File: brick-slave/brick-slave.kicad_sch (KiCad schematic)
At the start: 4 parts, among them J1 Conn_01x06_Male, J2 Conn_01x06_Male, J3 Conn_01x06_Female, J4 Conn_01x06_Female

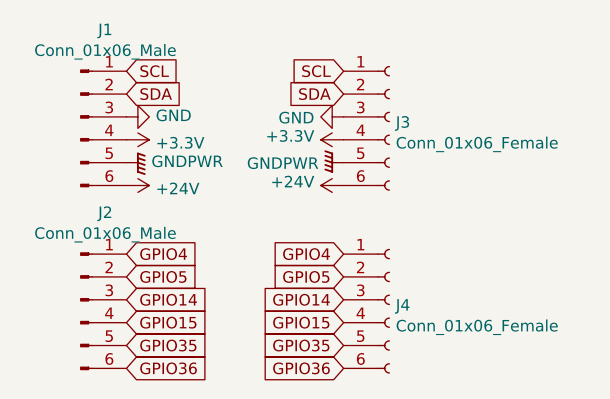
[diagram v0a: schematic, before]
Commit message: change PWR voltage
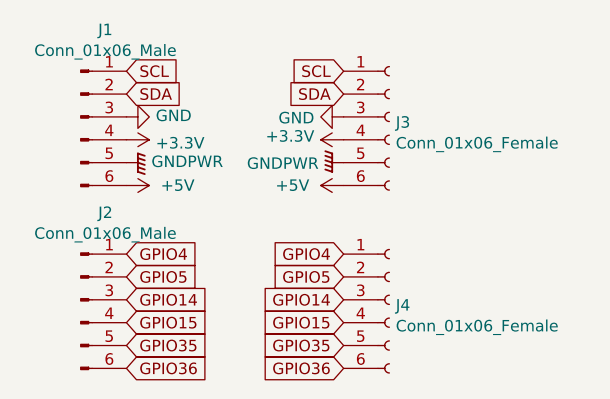
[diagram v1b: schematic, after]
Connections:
- net +24V renamed +5V
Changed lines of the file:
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@@
     (pin "1")
   )
-  (symbol (lib_id "power:+24V") (at 27.94 34.29 270) (unit 1)
-    (in_bom yes) (on_board yes)
-    (property "Reference" "#PWR04" (id 0) (at 24.13 34.29 0)
-      (effects (font (size 1.27 1.27)) hide)
-    )
-    (property "Value" "+24V" (id 1) (at 31.1912 34.671 90)
+  (symbol (lib_id "power:+5V") (at 27.94 34.29 270) (unit 1)
+    (in_bom yes) (on_board yes) (fields_autoplaced)
+    (property "Reference" "#PWR?" (id 0) (at 24.13 34.29 0)
+      (effects (font (size 1.27 1.27)) hide)
+    )
+    (property "Value" "+5V" (id 1) (at 31.75 34.2899 90)
       (effects (font (size 1.27 1.27)) (justify left))
     )
@@
     (pin "1")
   )
-  (symbol (lib_id "power:+24V") (at 52.07 34.29 90) (unit 1)
-    (in_bom yes) (on_board yes)
-    (property "Reference" "#PWR08" (id 0) (at 55.88 34.29 0)
-      (effects (font (size 1.27 1.27)) hide)
-    )
-    (property "Value" "+24V" (id 1) (at 48.8188 33.909 90)
+  (symbol (lib_id "power:+5V") (at 52.07 34.29 90) (unit 1)
+    (in_bom yes) (on_board yes) (fields_autoplaced)
+    (property "Reference" "#PWR?" (id 0) (at 55.88 34.29 0)
+      (effects (font (size 1.27 1.27)) hide)
+    )
+    (property "Value" "+5V" (id 1) (at 48.26 34.2899 90)
       (effects (font (size 1.27 1.27)) (justify left))
     )
@@
       (reference "#PWR03") (unit 1) (value "GNDPWR") (footprint "")
     )
-    (path "/00000000-0000-0000-0000-0000600deecd"
-      (reference "#PWR04") (unit 1) (value "+24V") (footprint "")
-    )
     (path "/00000000-0000-0000-0000-00005fa7a4aa"
       (reference "#PWR05") (unit 1) (value "GND") (footprint "")
@@
       (reference "#PWR07") (unit 1) (value "GNDPWR") (footprint "")
     )
-    (path "/00000000-0000-0000-0000-00005fa77315"
-      (reference "#PWR08") (unit 1) (value "+24V") (footprint "")
+    (path "/10ee8fca-8566-4cb1-b842-f5d8f533e542"
+      (reference "#PWR?") (unit 1) (value "+5V") (footprint "")
+    )
+    (path "/9bbfd4f7-70b4-4989-bf3c-db3bd5c855da"
+      (reference "#PWR?") (unit 1) (value "+5V") (footprint "")
     )
     (path "/00000000-0000-0000-0000-0000600e0e0c"

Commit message: refactor brick-slave
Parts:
- added H1, H2, H3, H4: MountingHole, MountingHole:MountingHole_3.2mm_M3, symbol Mechanical:MountingHole
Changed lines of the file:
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@@
   (symbol (lib_id "power:+5V") (at 27.94 34.29 270) (unit 1)
     (in_bom yes) (on_board yes) (fields_autoplaced)
-    (property "Reference" "#PWR?" (id 0) (at 24.13 34.29 0)
+    (property "Reference" "#PWR0101" (id 0) (at 24.13 34.29 0)
       (effects (font (size 1.27 1.27)) hide)
     )
@@
   (symbol (lib_id "power:+5V") (at 52.07 34.29 90) (unit 1)
     (in_bom yes) (on_board yes) (fields_autoplaced)
-    (property "Reference" "#PWR?" (id 0) (at 55.88 34.29 0)
+    (property "Reference" "#PWR0102" (id 0) (at 55.88 34.29 0)
       (effects (font (size 1.27 1.27)) hide)
     )
@@
     )
     (pin "1")
+  )
+  (symbol (lib_id "Mechanical:MountingHole") (at 264.16 20.32 0) (unit 1)
+    (in_bom yes) (on_board yes) (fields_autoplaced)
+    (property "Reference" "H1" (id 0) (at 267.97 19.0499 0)
+      (effects (font (size 1.27 1.27)) (justify left))
+    )
+    (property "Value" "MountingHole" (id 1) (at 267.97 21.5899 0)
+      (effects (font (size 1.27 1.27)) (justify left))
+    )
+    (property "Footprint" "MountingHole:MountingHole_3.2mm_M3" (id 2) (at 264.16 20.32 0)
+      (effects (font (size 1.27 1.27)) hide)
+    )
+    (property "Datasheet" "~" (id 3) (at 264.16 20.32 0)
+      (effects (font (size 1.27 1.27)) hide)
+    )
+  )
+  (symbol (lib_id "Mechanical:MountingHole") (at 264.16 25.4 0) (unit 1)
+    (in_bom yes) (on_board yes) (fields_autoplaced)
+    (property "Reference" "H2" (id 0) (at 267.97 24.1299 0)
+      (effects (font (size 1.27 1.27)) (justify left))
+    )
+    (property "Value" "MountingHole" (id 1) (at 267.97 26.6699 0)
+      (effects (font (size 1.27 1.27)) (justify left))
+    )
+    (property "Footprint" "MountingHole:MountingHole_3.2mm_M3" (id 2) (at 264.16 25.4 0)
+      (effects (font (size 1.27 1.27)) hide)
+    )
+    (property "Datasheet" "~" (id 3) (at 264.16 25.4 0)
+      (effects (font (size 1.27 1.27)) hide)
+    )
+  )
+  (symbol (lib_id "Mechanical:MountingHole") (at 264.16 30.48 0) (unit 1)
+    (in_bom yes) (on_board yes) (fields_autoplaced)
+    (property "Reference" "H3" (id 0) (at 267.97 29.2099 0)
+      (effects (font (size 1.27 1.27)) (justify left))
+    )
+    (property "Value" "MountingHole" (id 1) (at 267.97 31.7499 0)
+      (effects (font (size 1.27 1.27)) (justify left))
+    )
+    (property "Footprint" "MountingHole:MountingHole_3.2mm_M3" (id 2) (at 264.16 30.48 0)
+      (effects (font (size 1.27 1.27)) hide)
+    )
+    (property "Datasheet" "~" (id 3) (at 264.16 30.48 0)
+      (effects (font (size 1.27 1.27)) hide)
+    )
+  )
+  (symbol (lib_id "Mechanical:MountingHole") (at 264.16 35.56 0) (unit 1)
+    (in_bom yes) (on_board yes) (fields_autoplaced)
+    (property "Reference" "H4" (id 0) (at 267.97 34.2899 0)
+      (effects (font (size 1.27 1.27)) (justify left))
+    )
+    (property "Value" "MountingHole" (id 1) (at 267.97 36.8299 0)
+      (effects (font (size 1.27 1.27)) (justify left))
+    )
+    (property "Footprint" "MountingHole:MountingHole_3.2mm_M3" (id 2) (at 264.16 35.56 0)
+      (effects (font (size 1.27 1.27)) hide)
+    )
+    (property "Datasheet" "~" (id 3) (at 264.16 35.56 0)
+      (effects (font (size 1.27 1.27)) hide)
+    )
   )
   (symbol (lib_id "Connector:Conn_01x06_Male") (at 22.86 26.67 0) (unit 1)
@@
     )
     (path "/10ee8fca-8566-4cb1-b842-f5d8f533e542"
-      (reference "#PWR?") (unit 1) (value "+5V") (footprint "")
+      (reference "#PWR0101") (unit 1) (value "+5V") (footprint "")
     )
     (path "/9bbfd4f7-70b4-4989-bf3c-db3bd5c855da"
-      (reference "#PWR?") (unit 1) (value "+5V") (footprint "")
+      (reference "#PWR0102") (unit 1) (value "+5V") (footprint "")
+    )
+    (path "/8811c6d3-8a3f-4950-9ce4-043f2ffb45ab"
+      (reference "H1") (unit 1) (value "MountingHole") (footprint "MountingHole:MountingHole_3.2mm_M3")
+    )
+    (path "/b0d8ba3f-c878-4944-a39c-e68d4b1f154d"
+      (reference "H2") (unit 1) (value "MountingHole") (footprint "MountingHole:MountingHole_3.2mm_M3")
+    )
+    (path "/cd70851f-7e3d-40b1-bf36-ebd1c048fd1f"
+      (reference "H3") (unit 1) (value "MountingHole") (footprint "MountingHole:MountingHole_3.2mm_M3")
+    )
+    (path "/7bbaf512-ad3c-4edf-87bb-b6f93b9f12f0"
+      (reference "H4") (unit 1) (value "MountingHole") (footprint "MountingHole:MountingHole_3.2mm_M3")
     )
     (path "/00000000-0000-0000-0000-0000600e0e0c"
